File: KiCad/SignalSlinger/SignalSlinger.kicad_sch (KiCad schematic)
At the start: 60 parts, among them J101 Conn_01x02, J102 Conn_01x03, J103 Conn_01x02, J104 Conn_01x02, J105 Conn_01x04, J106 Conn_01x02, J107 DB9 Female, P101 ISP/PDI, Q101 BSS84W-7-F, Q102 BSS138W-7-F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

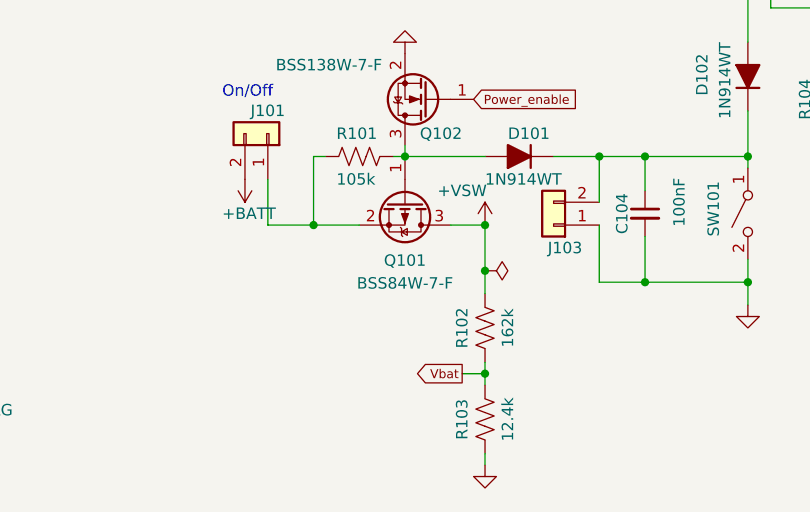
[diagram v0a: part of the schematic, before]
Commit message: BOM Corrections
o Updated BOM
o Updated Footprints
o Updated PCB and Gerbers
o Updated schematic
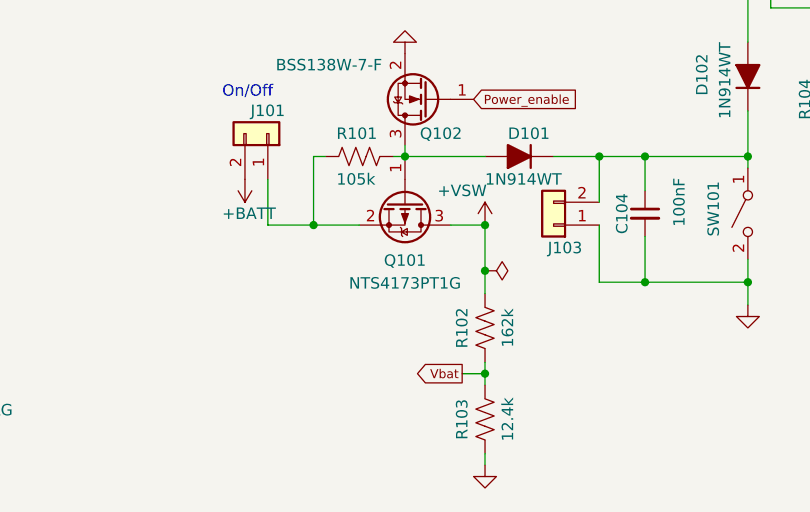
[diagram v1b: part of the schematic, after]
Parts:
- D107, D115: Digi-Key Part No. RB070MM-30CT-ND -> CRS09QCT-ND; Link https://www.digikey.com/en/products/detail/rohm-semiconduct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 -> (none); Manufacturer Rohm Semiconductor -> Toshiba Semiconductor and Storage; Manufacturer PN RB070MM-30TR -> CRS09(TE85L,Q,M)
- Q101: value BSS84W-7-F -> NTS4173PT1G; Digi-Key Part No. BSS84W-FDICT-ND -> NTS4173PT1GOSCT-ND; LCSC Part Number C110490 -> (none); Link https://www.digikey.com/short/fjvhfm07 -> https://www.digikey.com/short/j97zqh7v; Manufacturer Diodes Incorporated -> ONSEMI; Manufacturer PN BSS84W-7-F -> NTS4173PT1G
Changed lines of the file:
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@@
   (title_block
     (title "SignalSlinger")
-    (date "2024-06-12")
-    (rev "3.3")
+    (date "2024-06-13")
+    (rev "3.4")
   )
   (junction (at 154.94 81.28) (diameter 0) (color 0 0 0 0)
@@
     (in_bom yes) (on_board yes) (fields_autoplaced)
     (property "Reference" "Q101" (id 0) (at 67.31 170.3054 90))
-    (property "Value" "BSS84W-7-F" (id 1) (at 67.31 172.8423 90))
+    (property "Value" "NTS4173PT1G" (id 1) (at 67.31 172.8423 90))
     (property "Footprint" "Package_TO_SOT_SMD:SOT-323_SC-70" (id 2) (at 65.405 168.91 0)
       (effects (font (size 1.27 1.27) italic) (justify left) hide)
@@
       (effects (font (size 1.27 1.27)) (justify left) hide)
     )
-    (property "Digi-Key Part No." "BSS84W-FDICT-ND" (id 4) (at 67.31 163.83 0)
+    (property "Digi-Key Part No." "NTS4173PT1GOSCT-ND" (id 4) (at 67.31 163.83 0)
       (effects (font (size 1.27 1.27)) hide)
     )
-    (property "Manufacturer" "Diodes Incorporated" (id 5) (at 67.31 163.83 0)
+    (property "Manufacturer" "ONSEMI" (id 5) (at 67.31 163.83 0)
       (effects (font (size 1.27 1.27)) hide)
     )
-    (property "Manufacturer PN" "BSS84W-7-F" (id 6) (at 67.31 163.83 0)
+    (property "Manufacturer PN" "NTS4173PT1G" (id 6) (at 67.31 163.83 0)
       (effects (font (size 1.27 1.27)) hide)
     )
-    (property "Description" "MOSFET P-CH 50V 130MA SOT323" (id 7) (at 67.31 163.83 0)
+    (property "Description" "MOSFET P-CH 30V 1.2A SC70-3" (id 7) (at 67.31 163.83 0)
       (effects (font (size 1.27 1.27)) hide)
     )
-    (property "Link" "https://www.digikey.com/short/fjvhfm07" (id 8) (at 67.31 163.83 0)
-      (effects (font (size 1.27 1.27)) hide)
-    )
-    (property "LCSC Part Number" "C110490" (id 9) (at 67.31 163.83 0)
+    (property "Link" "https://www.digikey.com/short/j97zqh7v" (id 8) (at 67.31 163.83 0)
       (effects (font (size 1.27 1.27)) hide)
     )
@@
     (pin "1")
   )
-  (symbol (lib_id "Device:D_Schottky_Filled") (at 196.85 38.1 90) (unit 1)
-    (in_bom yes) (on_board yes)
-    (property "Reference" "D115" (id 0) (at 198.12 35.56 90)
-      (effects (font (size 1.27 1.27)) (justify right))
-    )
-    (property "Value" "Schottky Diode" (id 1) (at 199.2829 38.4175 0)
-      (effects (font (size 1.27 1.27)) hide)
-    )
-    (property "Footprint" "Diode_SMD:D_SOD-123FL" (id 2) (at 196.85 38.1 0)
-      (effects (font (size 1.27 1.27)) hide)
-    )
-    (property "Datasheet" "" (id 3) (at 196.85 38.1 0)
-      (effects (font (size 1.27 1.27)) hide)
-    )
-    (property "Digi-Key Part No." "RB070MM-30CT-ND" (id 4) (at 196.85 38.1 0)
-      (effects (font (size 1.27 1.27)) hide)
-    )
-    (property "Link" "https://www.digikey.com/en/products/detail/rohm-semiconductor/RB070MM-30TR/5001862" (id 5) (at 196.85 38.1 0)
-      (effects (font (size 1.27 1.27)) hide)
-    )
-    (property "Manufacturer" "Rohm Semiconductor" (id 6) (at 196.85 38.1 0)
-      (effects (font (size 1.27 1.27)) hide)
-    )
-    (property "Manufacturer PN" "RB070MM-30TR" (id 7) (at 196.85 38.1 0)
-      (effects (font (size 1.27 1.27)) hide)
-    )
-    (property "Description" "DIODE SCHOTTKY 30V 1.5A SOD-123FL" (id 8) (at 196.85 38.1 0)
-      (effects (font (size 1.27 1.27)) hide)
-    )
-    (pin "1")
-    (pin "2")
-  )
   (symbol (lib_id "Jumper:Jumper_2_Bridged") (at 252.73 58.42 270) (unit 1)
     (in_bom yes) (on_board yes) (fields_autoplaced)
@@
     (pin "1")
   )
+  (symbol (lib_id "Device:D_Schottky_Filled") (at 196.85 38.1 90) (unit 1)
+    (in_bom yes) (on_board yes)
+    (property "Reference" "D115" (id 0) (at 198.12 35.56 90)
+      (effects (font (size 1.27 1.27)) (justify right))
+    )
+    (property "Value" "Schottky Diode" (id 1) (at 199.2829 38.4175 0)
+      (effects (font (size 1.27 1.27)) hide)
+    )
+    (property "Footprint" "Diode_SMD:D_SOD-123FL" (id 2) (at 196.85 38.1 0)
+      (effects (font (size 1.27 1.27)) hide)
+    )
+    (property "Datasheet" "" (id 3) (at 196.85 38.1 0)
+      (effects (font (size 1.27 1.27)) hide)
+    )
+    (property "Digi-Key Part No." "CRS09QCT-ND" (id 4) (at 196.85 38.1 0)
+      (effects (font (size 1.27 1.27)) hide)
+    )
+    (property "Manufacturer" "Toshiba Semiconductor and Storage" (id 6) (at 196.85 38.1 0)
+      (effects (font (size 1.27 1.27)) hide)
+    )
+    (property "Manufacturer PN" "CRS09(TE85L,Q,M)" (id 7) (at 196.85 38.1 0)
+      (effects (font (size 1.27 1.27)) hide)
+    )
+    (property "Description" "DIODE SCHOTTKY 30V 1.5A SOD-123FL" (id 8) (at 196.85 38.1 0)
+      (effects (font (size 1.27 1.27)) hide)
+    )
+    (pin "1")
+    (pin "2")
+  )
   (symbol (lib_id "Connector:TEST_SCOPE") (at 209.55 93.98 90) (unit 1)
     (in_bom yes) (on_board yes)
@@
       (effects (font (size 1.27 1.27)) hide)
     )
-    (property "Digi-Key Part No." "RB070MM-30CT-ND" (id 4) (at 191.77 38.1 0)
+    (property "Digi-Key Part No." "CRS09QCT-ND" (id 4) (at 191.77 38.1 0)
       (effects (font (size 1.27 1.27)) hide)
     )
-    (property "Link" "https://www.digikey.com/en/products/detail/rohm-semiconductor/RB070MM-30TR/5001862" (id 5) (at 191.77 38.1 0)
+    (property "Manufacturer" "Toshiba Semiconductor and Storage" (id 6) (at 191.77 38.1 0)
       (effects (font (size 1.27 1.27)) hide)
     )
-    (property "Manufacturer" "Rohm Semiconductor" (id 6) (at 191.77 38.1 0)
-      (effects (font (size 1.27 1.27)) hide)
-    )
-    (property "Manufacturer PN" "RB070MM-30TR" (id 7) (at 191.77 38.1 0)
+    (property "Manufacturer PN" "CRS09(TE85L,Q,M)" (id 7) (at 191.77 38.1 0)
       (effects (font (size 1.27 1.27)) hide)
     )
@@
       (reference "C304") (unit 1) (value "91pF") (footprint "Capacitor_SMD:C_0805_2012Metric")
     )
-    (path "/da189f43-fd1f-445a-980b-345fda8b9a74/8051eae5-ac4d-4d42-9a96-9e97374cb109"
+    (path "/da189f43-fd1f-445a-980b-345fda8b9a74/2f5d0f80-d906-427a-b562-7c3210c6805d"
       (reference "C305") (unit 1) (value "1100pF") (footprint "Capacitor_SMD:C_0805_2012Metric")
     )
@@
       (reference "D112") (unit 1) (value "ESD9B5.0ST5G_1") (footprint "Diode_SMD:D_0603_1608Metric")
     )
-    (path "/5eba5dba-24e0-4969-94b7-4be7176f58ba"
+    (path "/a9a36a75-420d-49ce-9062-e6b204c29358"
       (reference "D115") (unit 1) (value "Schottky Diode") (footprint "Diode_SMD:D_SOD-123FL")
     )
@@
     )
     (path "/b7c888bf-e50e-45b8-8886-9bc5abf637fe/67c41640-a5e7-4fd7-a17b-9c7fc94c4026"
-      (reference "D202") (unit 1) (value "B330A Schottky Diode") (footprint "Diode_SMD:D_SMB")
+      (reference "D202") (unit 1) (value "B330A Schottky Diode") (footprint "Diode_SMD:D_SMA")
     )
-    (path "/b7c888bf-e50e-45b8-8886-9bc5abf637fe/698ef3e5-c802-45b7-80dd-701416eb8328"
+    (path "/b7c888bf-e50e-45b8-8886-9bc5abf637fe/0dfa7599-218c-47d4-be01-a8f78bd1d912"
       (reference "D203") (unit 1) (value "Schottky Diode") (footprint "Diode_SMD:D_SOD-123FL")
     )
-    (path "/b7c888bf-e50e-45b8-8886-9bc5abf637fe/4f3ddfea-cbf3-4ab3-8882-24e9d1905728"
+    (path "/b7c888bf-e50e-45b8-8886-9bc5abf637fe/bd3260fb-6f13-4ed2-bf2a-b327da80acae"
       (reference "D204") (unit 1) (value "Schottky Diode") (footprint "Diode_SMD:D_SOD-123FL")
     )
-    (path "/b7c888bf-e50e-45b8-8886-9bc5abf637fe/87b056ce-c433-4082-bd07-29a24fd1dfc2"
+    (path "/b7c888bf-e50e-45b8-8886-9bc5abf637fe/39a39792-8398-4a60-bec3-9e28b759a61f"
       (reference "D206") (unit 1) (value "Schottky Diode") (footprint "Diode_SMD:D_SOD-123FL")
     )
-    (path "/b7c888bf-e50e-45b8-8886-9bc5abf637fe/91d911d5-cad3-4a98-ba2b-306af461b4c4"
+    (path "/b7c888bf-e50e-45b8-8886-9bc5abf637fe/0b6c997b-2ae3-4fe1-8412-36b6738b871c"
       (reference "D207") (unit 1) (value "Schottky Diode") (footprint "Diode_SMD:D_SOD-123FL")
     )
@@
       (reference "JP203") (unit 1) (value "Ext-to-Boost") (footprint "Jumper:SolderJumper-2_P1.3mm_Bridged_RoundedPad1.0x1.5mm")
     )
+    (path "/b7c888bf-e50e-45b8-8886-9bc5abf637fe/068370c8-d635-4b09-b7f8-4271634b0d99"
+      (reference "JP204") (unit 1) (value "Internal_V_Enable") (footprint "Jumper:SolderJumper-2_P1.3mm_Open_RoundedPad1.0x1.5mm")
+    )
     (path "/4ce4bf50-5c77-4c5d-a0ee-ed9a4794ecf5"
       (reference "L101") (unit 1) (value "9T #24 Bifilar T50-43") (footprint "Inductors:Toroid_T-50A_TH_BF_CT_Vertical")
@@
     )
     (path "/06bbe3d7-7cbc-4293-aa1a-7cb3a9e9e8b9"
-      (reference "Q101") (unit 1) (value "BSS84W-7-F") (footprint "Package_TO_SOT_SMD:SOT-323_SC-70")
+      (reference "Q101") (unit 1) (value "NTS4173PT1G") (footprint "Package_TO_SOT_SMD:SOT-323_SC-70")
     )
     (path "/c8819402-7151-4b21-9689-27976a72a03f"

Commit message: Button Tweak
o Updated on-PCB pushbutton to be the same one used for SignalSnagger
o Updated location of pushbutton to reach only to the edge of the PCB
o Updated Gerbers
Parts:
- SW101: value SW_SPST -> (none); footprint Button_Switch_SMD:SW_SPST_TL3305A -> (none)
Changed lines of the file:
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@@
       (effects (font (size 1.27 1.27)) (justify right))
     )
-    (property "Value" "SW_SPST" (id 1) (at 106.553 166.8022 90)
+    (property "Value" "" (id 1) (at 106.553 166.8022 90)
       (effects (font (size 1.27 1.27)) (justify right) hide)
     )
-    (property "Footprint" "Button_Switch_SMD:SW_SPST_TL3305A" (id 2) (at 105.41 165.1 0)
+    (property "Footprint" "" (id 2) (at 105.41 165.1 0)
       (effects (font (size 1.27 1.27)) hide)
     )
@@
     )
     (path "/8753d621-69e1-4251-a22d-f8eaf42e9c5c"
-      (reference "SW101") (unit 1) (value "SW_SPST") (footprint "Button_Switch_SMD:SW_SPST_TL3305A")
+      (reference "SW101") (unit 1) (value "SW_SPST") (footprint "Button_Switch_SMD:SW_SPST_TL1014BF160QG")
     )
     (path "/266895fa-6ad4-44ed-bb39-fadda6cfebc1"

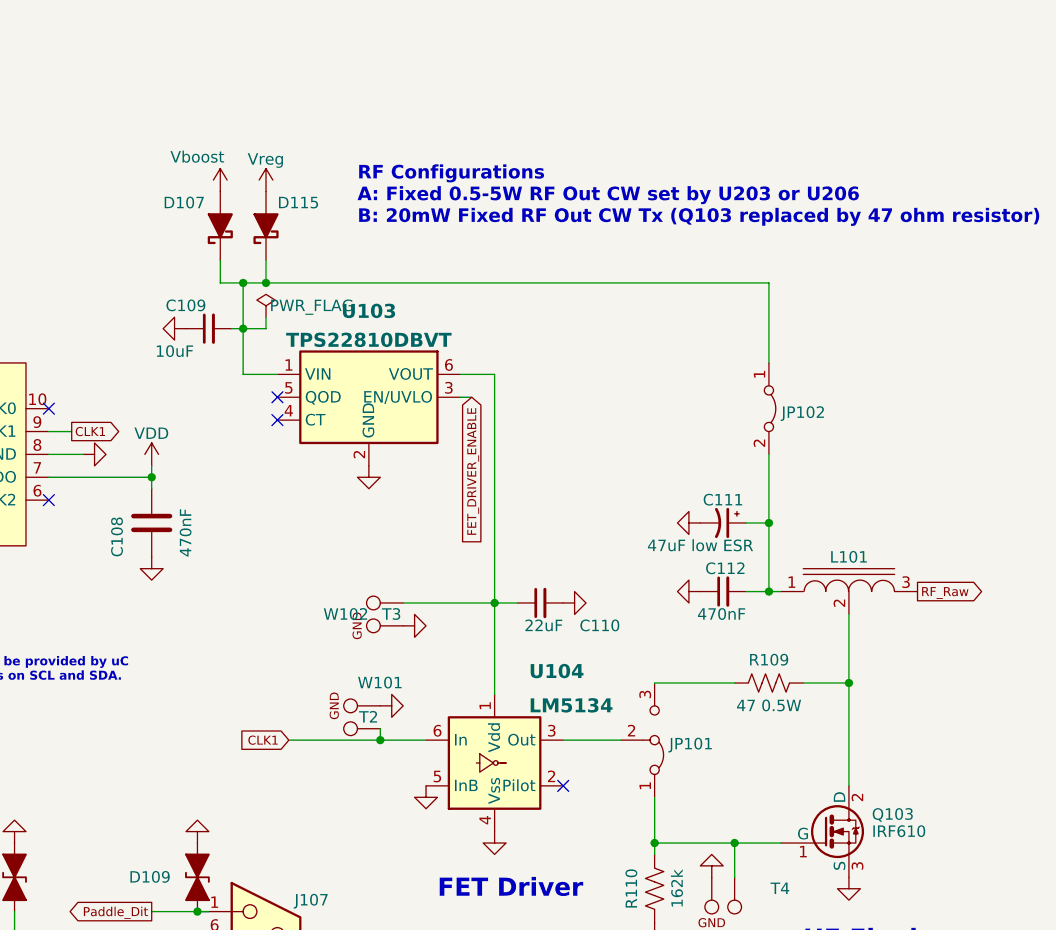
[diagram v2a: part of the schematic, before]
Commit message: Updated to Latest KiCad Version
Updated files
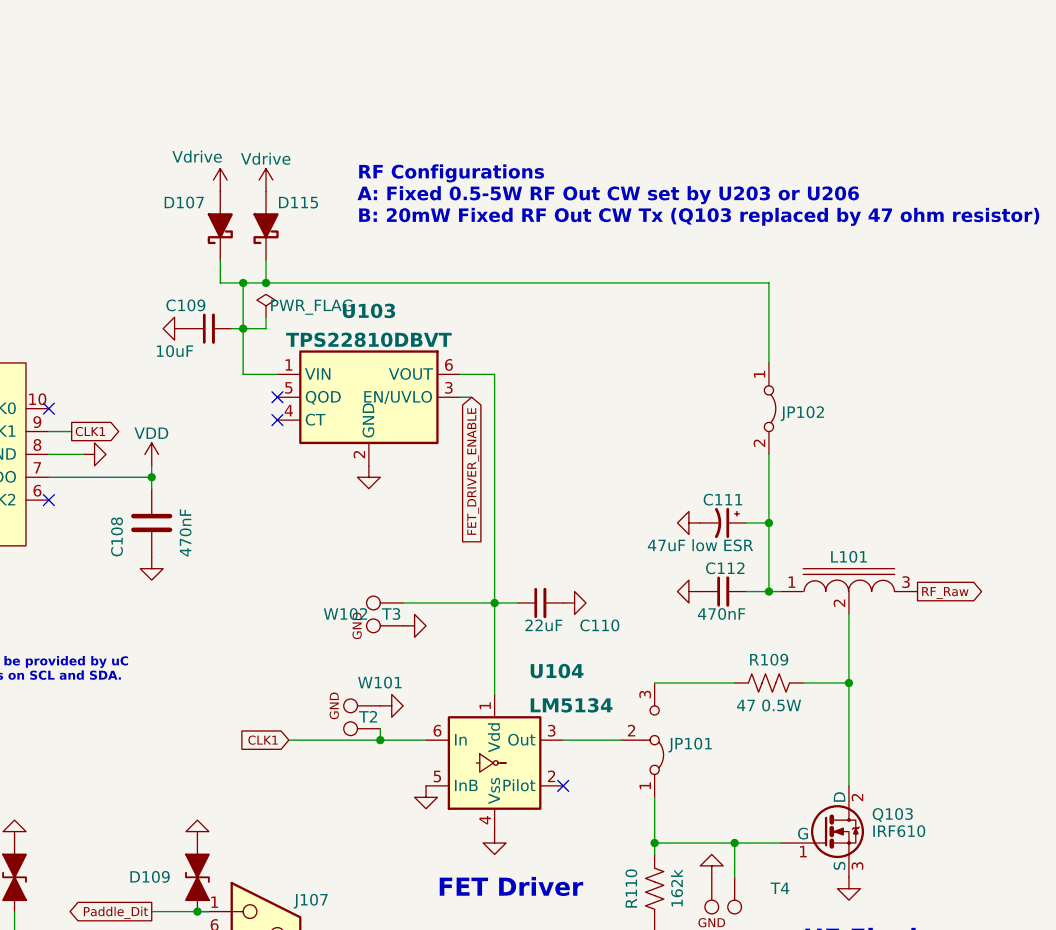
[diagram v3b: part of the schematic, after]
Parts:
- SW101: value (none) -> SW_SPST; footprint (none) -> Button_Switch_SMD:SW_SPST_TL1014BF160QG
